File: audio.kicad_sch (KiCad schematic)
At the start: 52 parts, among them J10 NCJ6FA-H-0, J9 NCJ6FA-H-0, Q2 2N3904, Q3 2N3904, Q4 2N3906, Q5 2N3906, U10 OPA1656ID, U11 LM2903, U8 THAT1246, U9 THAT1246

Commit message: starting on output
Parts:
- C20, C22, C24, C26: value 10u -> C
- C21, C23, C25, C27, C28, C30, C32, C33: value 100n -> C
- C29, C31: value 1n -> C
- C34, C35, C36, C37: value 47u -> C
- Q2, Q3, Q4, Q5: footprint Package_TO_SOT_SMD:SOT-23 -> Package_TO_SOT_THT:TO-92_Inline
- R19, R20, R27, R30, R31, R34: value 10k 1% -> R
- R21, R22: value 12k 1% -> R
- R23, R24: value 3k3 -> R
- R25, R26: value 1k -> R
- R28, R29, R32, R33: value 1k5 1% -> R
- RV5, RV6: value 10k -> R_Potentiometer_Trim
- TP1: value IN-R -> TestPoint
- TP2: value IN-L -> TestPoint
- TP3: value +LCLAMP -> TestPoint
- TP4: value -LCLAMP -> TestPoint
- TP5: value +RCLAMP -> TestPoint
- TP6: value -RCLAMP -> TestPoint
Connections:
- net +12VA: no longer U8.7 (Vcc/V+), U9.7 (Vcc/V+)
- net GND: now also U8.7 (Vcc/V+), U9.7 (Vcc/V+); no longer U8.1 (Ref), U9.1 (Ref)
- net at J10.3, J10.R: no longer U9.2 (In-)
- net at J10.2, J10.T: no longer U9.3 (In+)
- net at J9.2, J9.T: no longer U8.3 (In+)
- net at J9.3, J9.R: no longer U8.2 (In-)

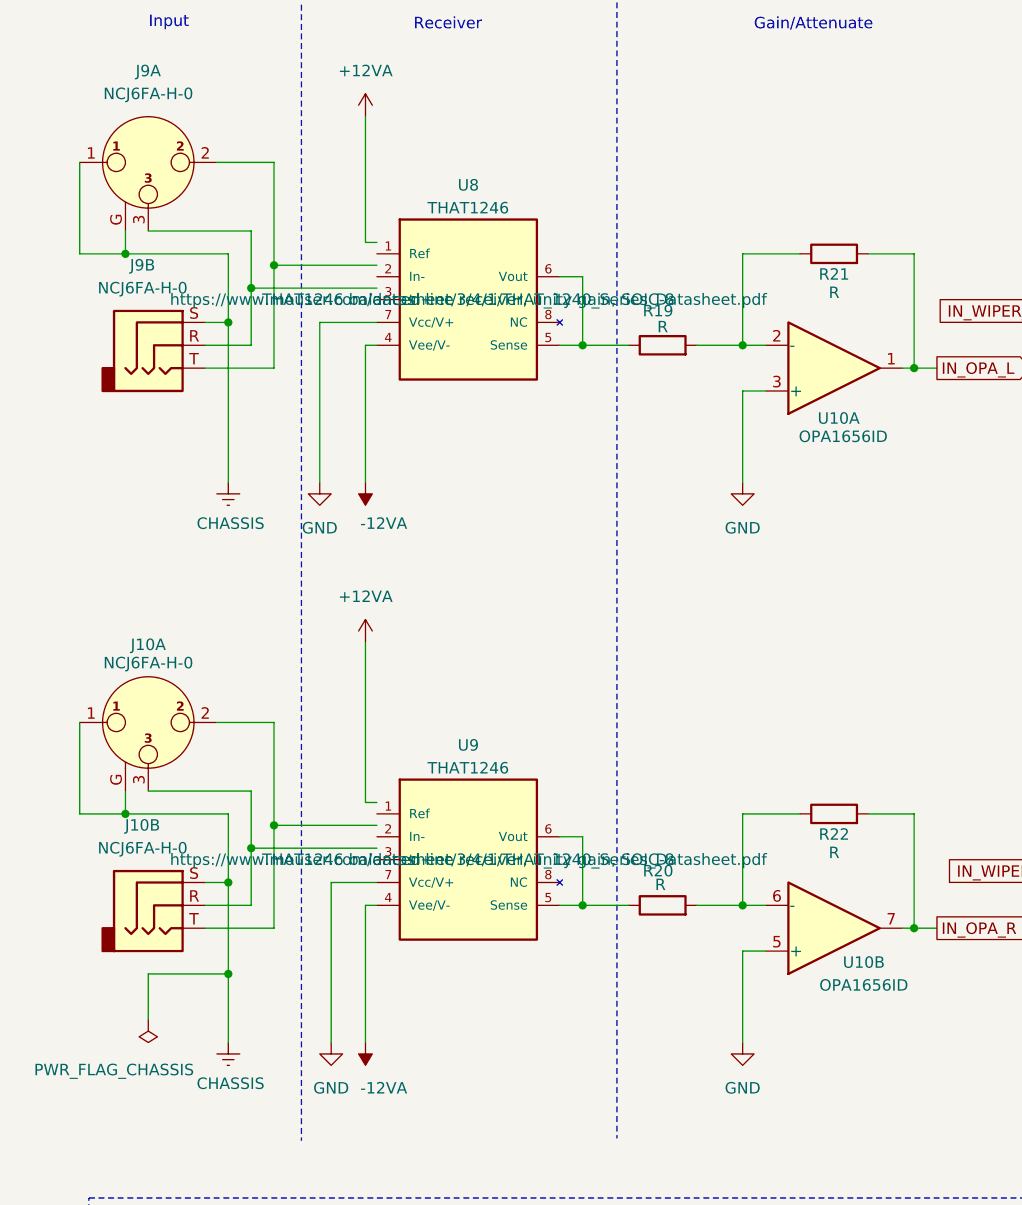
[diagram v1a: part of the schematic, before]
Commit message: daughterboard added
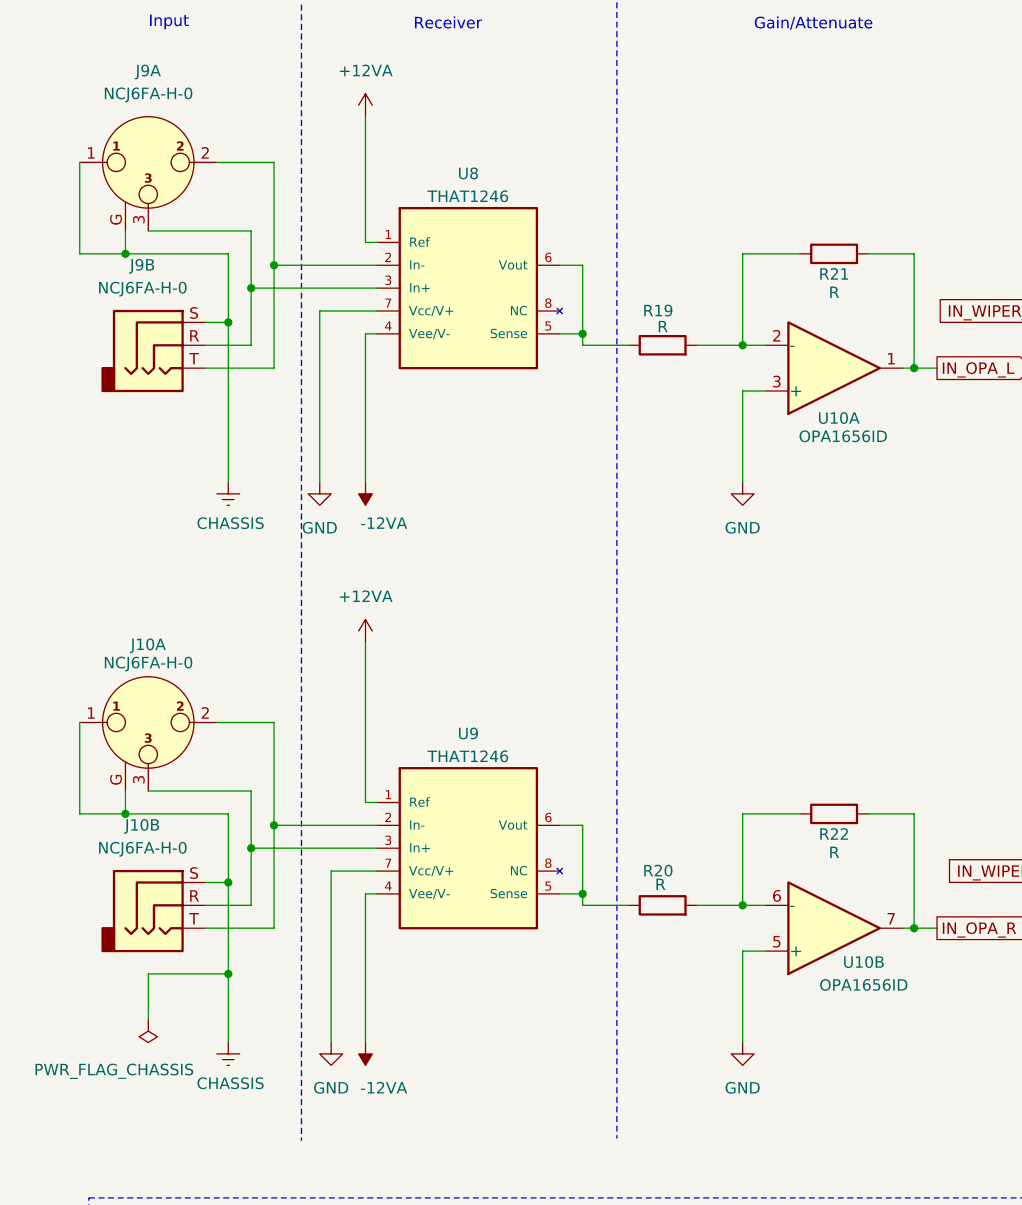
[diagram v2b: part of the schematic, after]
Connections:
- net +12VA: now also U8.1 (Ref), U9.1 (Ref)
- net at J10.3, J10.R: now also U9.3 (In+)
- net at J10.2, J10.T: now also U9.2 (In-)
- net at J9.2, J9.T: now also U8.2 (In-)
- net at J9.3, J9.R: now also U8.3 (In+)
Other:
- moved on the sheet: U8, U9
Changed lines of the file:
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@@
 	)
 	(junction
-		(at 72.39 53.34)
-		(diameter 0)
-		(color 0 0 0 0)
-	)
-	(junction
 		(at 198.12 49.53)
 		(diameter 0)
@@
 	)
 	(junction
-		(at 72.39 115.57)
-		(diameter 0)
-		(color 0 0 0 0)
-	)
-	(junction
 		(at 21.59 105.41)
 		(diameter 0)
@@
 	)
 	(junction
+		(at 72.39 52.07)
+		(diameter 0)
+		(color 0 0 0 0)
+	)
+	(junction
 		(at 238.76 39.37)
 		(diameter 0)
@@
 	)
 	(junction
+		(at 72.39 114.3)
+		(diameter 0)
+		(color 0 0 0 0)
+	)
+	(junction
 		(at 229.87 151.13)
 		(diameter 0)
@@
 	(wire
 		(pts
-			(xy 69.85 107.95) (xy 72.39 107.95)
+			(xy 69.85 106.68) (xy 72.39 106.68)
 		)
 		(stroke
@@
 	(wire
 		(pts
+			(xy 72.39 52.07) (xy 72.39 53.34)
+		)
+		(stroke
+			(width 0)
+			(type default)
+		)
+	)
+	(wire
+		(pts
 			(xy 251.46 140.97) (xy 251.46 142.24)
 		)
@@
 	(wire
 		(pts
-			(xy 44.45 113.03) (xy 44.45 130.81)
+			(xy 44.45 111.76) (xy 44.45 130.81)
 		)
 		(stroke
@@
 	(wire
 		(pts
-			(xy 72.39 107.95) (xy 72.39 115.57)
+			(xy 72.39 106.68) (xy 72.39 114.3)
 		)
 		(stroke
@@
 	(wire
 		(pts
-			(xy 69.85 53.34) (xy 72.39 53.34)
+			(xy 69.85 52.07) (xy 72.39 52.07)
 		)
 		(stroke
@@
 	(wire
 		(pts
-			(xy 49.53 113.03) (xy 44.45 113.03)
+			(xy 49.53 111.76) (xy 44.45 111.76)
 		)
 		(stroke
@@
 	(wire
 		(pts
-			(xy 48.26 115.57) (xy 49.53 115.57)
+			(xy 48.26 114.3) (xy 49.53 114.3)
 		)
 		(stroke
@@
 	(wire
 		(pts
-			(xy 43.18 50.8) (xy 43.18 68.58)
+			(xy 43.18 49.53) (xy 43.18 68.58)
 		)
 		(stroke
@@
 	(wire
 		(pts
-			(xy 69.85 45.72) (xy 72.39 45.72)
+			(xy 69.85 44.45) (xy 72.39 44.45)
 		)
 		(stroke
@@
 	(wire
 		(pts
-			(xy 48.26 130.81) (xy 48.26 115.57)
+			(xy 48.26 130.81) (xy 48.26 114.3)
 		)
 		(stroke
@@
 	(wire
 		(pts
-			(xy 48.26 53.34) (xy 49.53 53.34)
+			(xy 48.26 52.07) (xy 49.53 52.07)
 		)
 		(stroke
@@
 	(wire
 		(pts
-			(xy 49.53 50.8) (xy 43.18 50.8)
+			(xy 49.53 49.53) (xy 43.18 49.53)
 		)
 		(stroke
@@
 	(wire
 		(pts
-			(xy 72.39 45.72) (xy 72.39 53.34)
+			(xy 72.39 44.45) (xy 72.39 52.07)
 		)
 		(stroke
@@
 	(wire
 		(pts
+			(xy 72.39 114.3) (xy 72.39 115.57)
+		)
+		(stroke
+			(width 0)
+			(type default)
+		)
+	)
+	(wire
+		(pts
 			(xy 35.56 102.87) (xy 24.13 102.87)
 		)
@@
 	(wire
 		(pts
-			(xy 69.85 115.57) (xy 72.39 115.57)
+			(xy 69.85 114.3) (xy 72.39 114.3)
 		)
 		(stroke
@@
 	(wire
 		(pts
-			(xy 48.26 68.58) (xy 48.26 53.34)
+			(xy 48.26 68.58) (xy 48.26 52.07)
 		)
 		(stroke
@@
 	(symbol
 		(lib_id "daisy-studio:THAT1246")
-		(at 59.69 110.49 0)
+		(at 59.69 109.22 0)
 		(unit 1)
 		(exclude_from_sim no)
@@
 		(dnp no)
 		(property "Reference" "U9"
-			(at 59.69 97.79 0)
+			(at 59.69 96.52 0)
 			(effects
 				(font
@@
 		)
 		(property "Value" "THAT1246"
-			(at 59.69 100.33 0)
+			(at 59.69 99.06 0)
 			(effects
 				(font
@@
 		)
 		(property "Footprint" "Package_SO:SOIC-8_3.9x4.9mm_P1.27mm"
-			(at 59.69 123.19 0)
+			(at 59.69 121.92 0)
 			(effects
 				(font
@@
 		)
 		(property "Datasheet" "https://www.mouser.com/datasheet/3/4/1/THAT_1240_Series_Datasheet.pdf"
-			(at 59.69 110.49 0)
+			(at 59.69 109.22 0)
 			(effects
 				(font
 					(size 1.27 1.27)
 				)
+				(hide yes)
 			)
 		)
 		(property "Description" "THAT1246 balanced line receiver, unity gain, SOIC-8"
-			(at 59.69 110.49 0)
+			(at 59.69 109.22 0)
 			(effects
 				(font
 					(size 1.27 1.27)
 				)
+				(hide yes)
 			)
 		)
 		(property "Placement" "Near input connector. Pins 1,4 to analog ground, keep ground path short and clean."
-			(at 59.69 110.49 0)
+			(at 59.69 109.22 0)
 			(effects
 				(font
@@
 	(symbol
 		(lib_id "daisy-studio:THAT1246")
-		(at 59.69 48.26 0)
+		(at 59.69 46.99 0)
 		(unit 1)
 		(exclude_from_sim no)
@@
 		(dnp no)
 		(property "Reference" "U8"
-			(at 59.69 35.56 0)
+			(at 59.69 34.29 0)
 			(effects
 				(font
@@
 		)
 		(property "Value" "THAT1246"
-			(at 59.69 38.1 0)
+			(at 59.69 36.83 0)
 			(effects
 				(font
@@
 		)
 		(property "Footprint" "Package_SO:SOIC-8_3.9x4.9mm_P1.27mm"
-			(at 59.69 60.96 0)
+			(at 59.69 59.69 0)
 			(effects
 				(font
@@
 		)
 		(property "Datasheet" "https://www.mouser.com/datasheet/3/4/1/THAT_1240_Series_Datasheet.pdf"
-			(at 59.69 48.26 0)
+			(at 59.69 46.99 0)
 			(effects
 				(font
 					(size 1.27 1.27)
 				)
+				(hide yes)
 			)
 		)
 		(property "Description" "THAT1246 balanced line receiver, unity gain, SOIC-8"
-			(at 59.69 48.26 0)
+			(at 59.69 46.99 0)
 			(effects
 				(font
 					(size 1.27 1.27)
 				)
+				(hide yes)
 			)
 		)
 		(property "Placement" "Near input connector. Pins 1,4 to analog ground, keep ground path short and clean."
-			(at 59.69 48.26 0)
+			(at 59.69 46.99 0)
 			(effects
 				(font

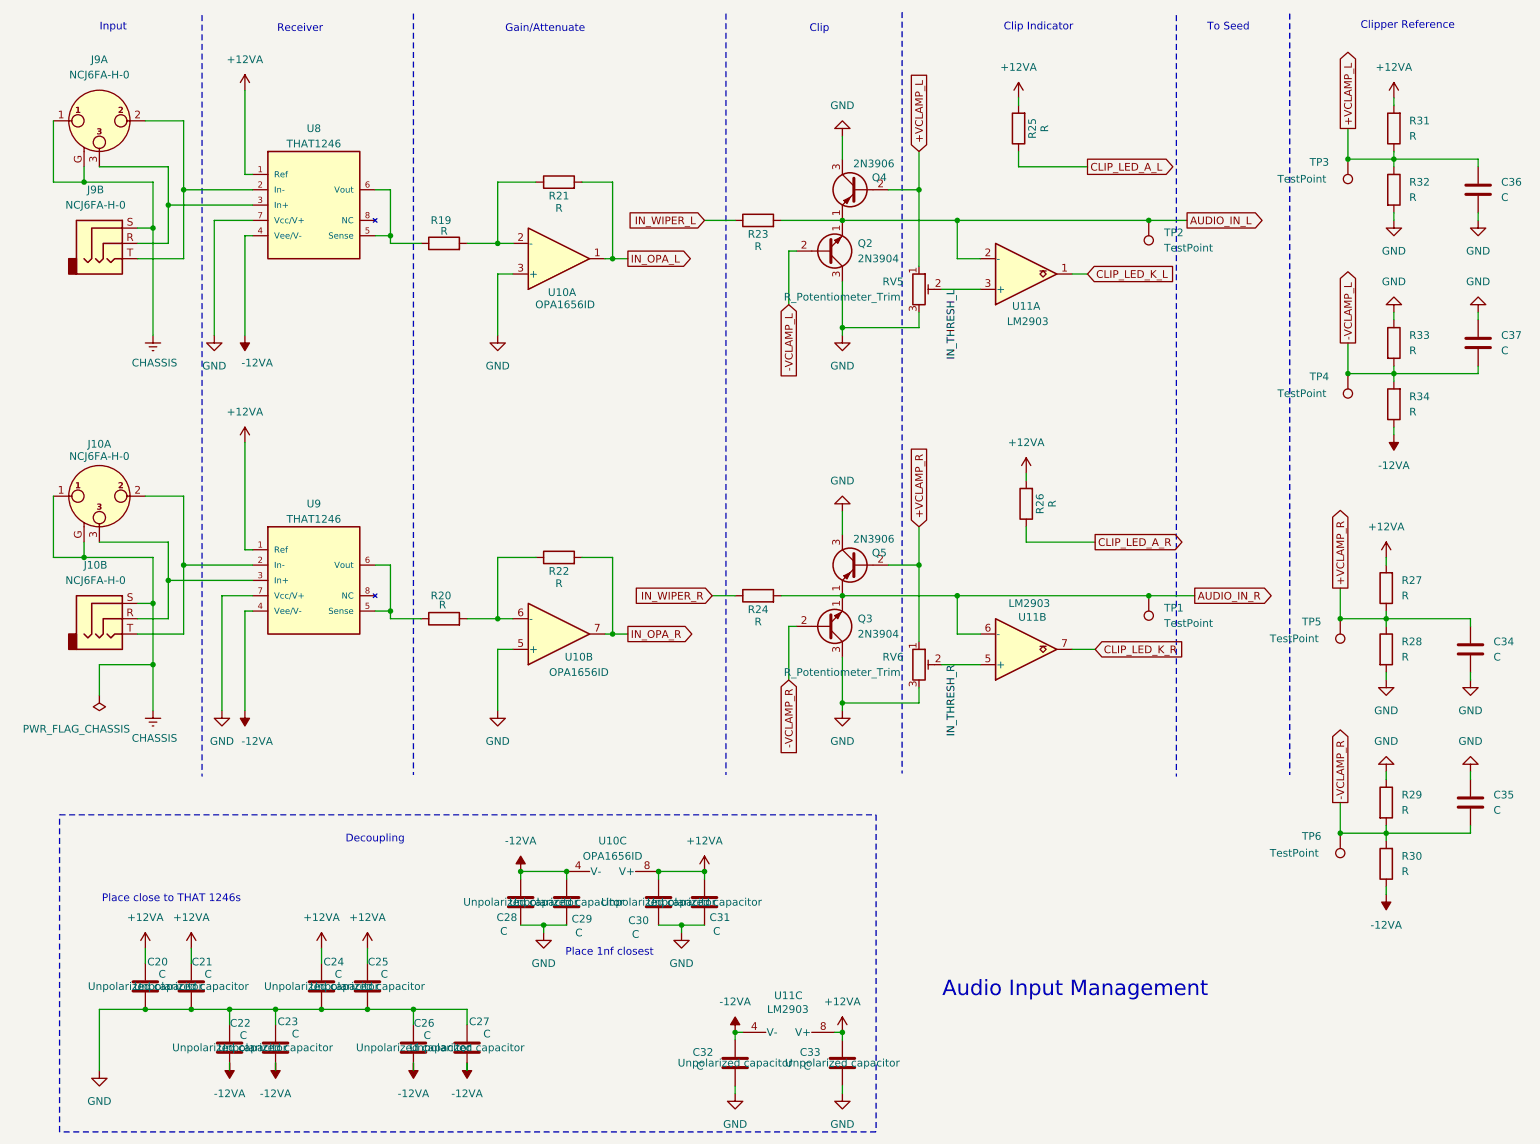
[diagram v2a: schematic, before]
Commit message: WIP trying to fix symbols and finish daughterboard
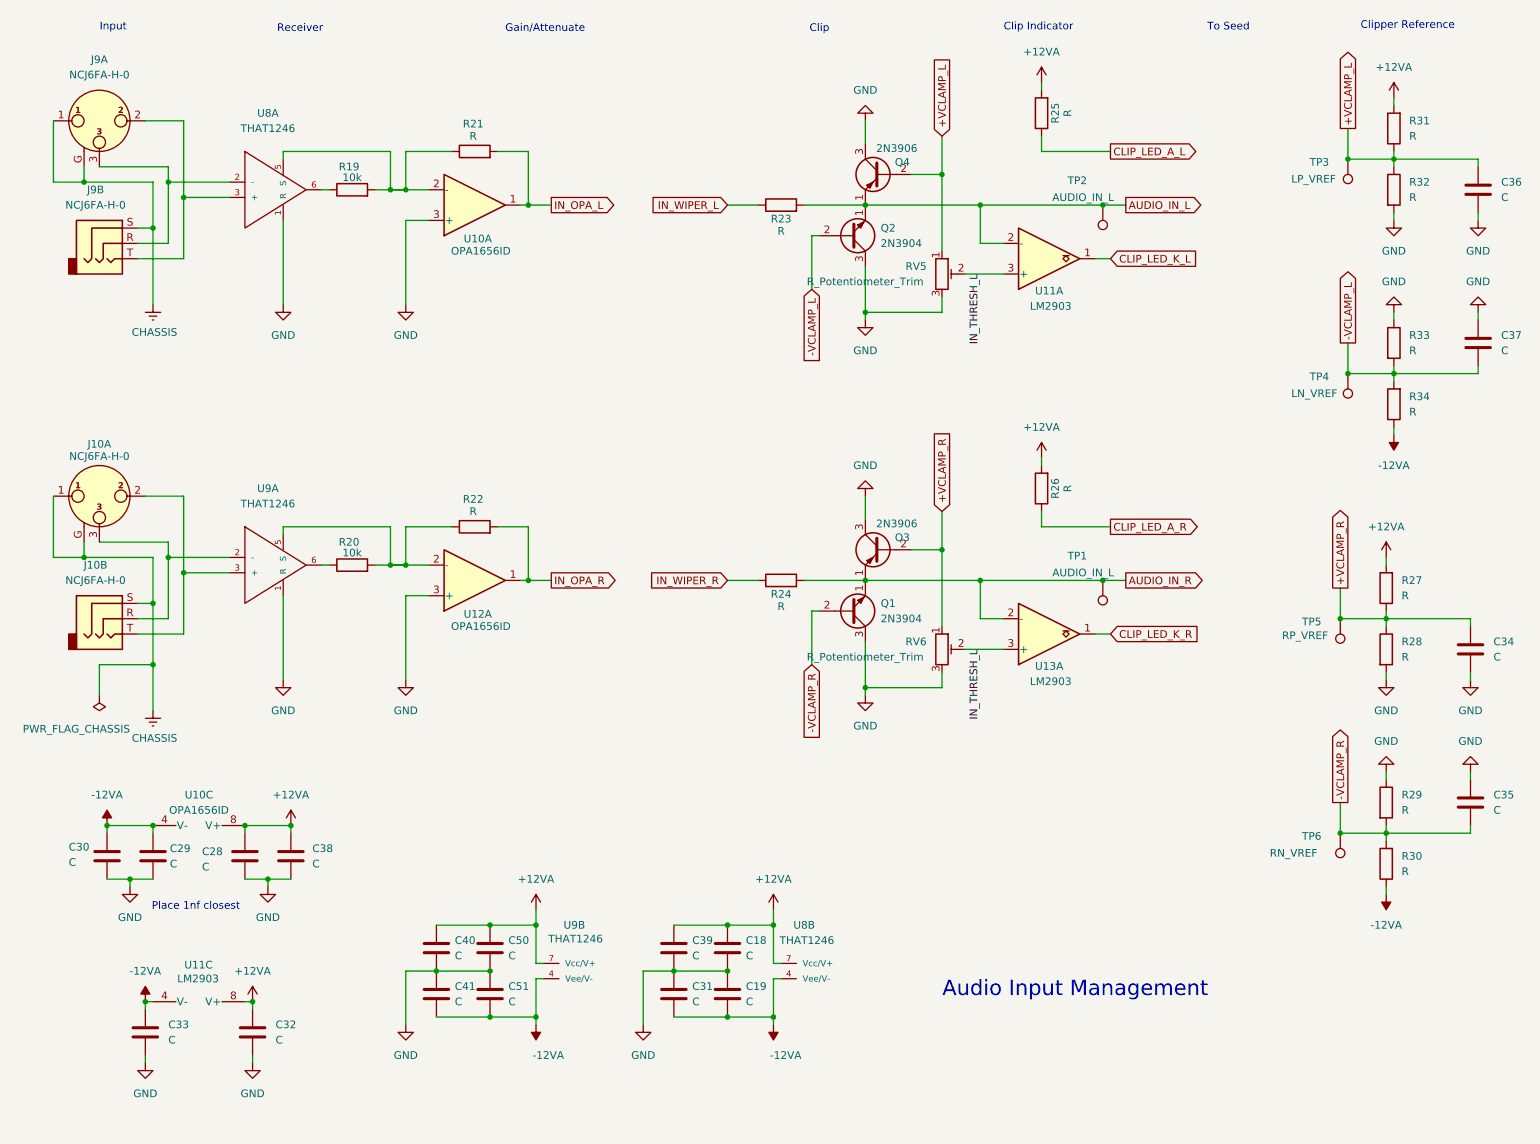
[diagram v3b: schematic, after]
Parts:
- removed C20, C21, C22, C23, C24, C25, C26, C27: C, Capacitor_SMD:C_0805_2012Metric, symbol Device:C
- removed Q3: 2N3904, Package_TO_SOT_THT:TO-92_Inline, symbol Transistor_BJT:2N3904
- removed Q5: 2N3906, Package_TO_SOT_THT:TO-92_Inline, symbol Transistor_BJT:2N3906
- removed unit 2 of U10
- removed unit 2 of U11
- removed U9: THAT1246, Package_SO:SOIC-8_3.9x4.9mm_P1.27mm, symbol daisy-studio:THAT1246
- added C18, C19, C38, C39, C40, C41, C50, C51: C, symbol Device:C
- added Q1: 2N3904, Package_TO_SOT_THT:TO-92_Inline, symbol Transistor_BJT:2N3904
- added Q3: 2N3906, Package_TO_SOT_THT:TO-92_Inline, symbol Transistor_BJT:2N3906
- added U12: OPA1656ID, Package_SO:SOIC-8_3.9x4.9mm_P1.27mm, symbol Amplifier_Operational:OPA1656ID
- added U13: LM2903, symbol Comparator:LM2903
- added U9: THAT1246, Package_SO:SOIC-8_3.9x4.9mm_P1.27mm, symbol daisy-studio:THAT1246
- C28, C29, C30, C31, C32, C33: footprint Capacitor_SMD:C_0805_2012Metric -> (none)
- R19, R20: value R -> 10k
- TP1, TP2: value TestPoint -> AUDIO_IN_L
- TP3: value TestPoint -> LP_VREF
- TP4: value TestPoint -> LN_VREF
- TP5: value TestPoint -> RP_VREF
- TP6: value TestPoint -> RN_VREF
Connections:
- net IN_THRESH_R is gone; now on net IN_THRESH_L: RV6.2
- net +12VA: now also C28.1, C32.1, U8.7 (Vcc/V+), C18.1, C38.1, C39.1, C40.1, C50.1, U9.7 (Vcc/V+); no longer C30.1, C31.1, C33.1, U8.1 (Ref)
- net +VCLAMP_R: now also Q3.2 (B)
- net -12VA: now also C30.1, C31.2, C33.1, C19.2, C41.2, C51.2, U9.4 (Vee/V-); no longer C28.1, C32.1
- net -VCLAMP_R: now also Q1.2 (B)
- net AUDIO_IN_R: now also Q1.1 (E), Q3.1 (E), U13.2 (-)
- net CLIP_LED_K_R: now also U13.1
- net GND: now also C31.1, U8.1 (R), C18.2, C19.1, C38.2, C39.2, C40.2, C41.1, C50.2, C51.1, Q1.3 (C), Q3.3 (C), U12.3 (+), U9.1 (R); no longer C31.2, U8.7 (Vcc/V+)
- net IN_OPA_R: now also U12.1
- net IN_THRESH_L: now also U13.3 (+)
- net at J10.3, J10.R: now also U9.2 (-)
- net at J10.2, J10.T: now also U9.3 (+)
- net at R20.2, R22.1: now also U12.2 (-), U9.5 (S)
- net at J9.2, J9.T: now also U8.3 (+); no longer U8.2 (In-)
- net at J9.3, J9.R: now also U8.2 (-); no longer U8.3 (In+)
- net at R20.1: now also U9.6
- net at R19.1, U8.6: no longer U8.5 (Sense)
- net at R19.2, R21.1, U10.2 (-): now also U8.5 (S)
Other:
- note removed: "Decoupling"
- note removed: "Place close to THAT 1246s"
- moved on the sheet: Q2, Q4, R19, R21, R23, R25, RV5, TP2, U10A, U10C, U11A, U11C

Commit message: WIP adding values
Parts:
- removed U12: OPA1656ID, Package_SO:SOIC-8_3.9x4.9mm_P1.27mm, symbol Amplifier_Operational:OPA1656ID
- removed U13: LM2903, symbol Comparator:LM2903
- added unit 2 of U10
- added unit 1 of U11
- added unit 1 of U8
- added unit 2 of U9
- C18, C19, C30, C32, C33, C38, C50, C51: value C -> 100n
- C28, C29: value C -> 1n
- C31, C39, C40, C41: value C -> 10u
- C34, C35, C36, C37: value C -> 47u
- R21, R22: value R -> 12k 1%
- R23, R24: value R -> 3.3k 1%
- R25, R26: value R -> 1k
- R27, R30, R31, R34: value R -> 10k 1%
- R28, R29, R32, R33: value R -> 1.5k 1%
- RV5, RV6: value R_Potentiometer_Trim -> 10k
- TP1: value AUDIO_IN_L -> AUDIO_IN_R
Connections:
- net +12VA: now also U9.7 (Vcc/V+); no longer U9.7 (Vcc/V+)
- net -12VA: now also U9.4 (Vee/V-); no longer U9.4 (Vee/V-)
- net AUDIO_IN_L: now also U11.2 (-); no longer U11.2 (-)
- net AUDIO_IN_R: now also U11.6 (-)
- net CLIP_LED_K_L: now also U11.1; no longer U11.1
- net CLIP_LED_K_R: now also U11.7
- net GND: now also U10.5 (+), U8.1 (R); no longer U8.1 (R)
- net IN_OPA_R: now also U10.7
- net IN_THRESH_L: now also U11.5 (+), U11.3 (+); no longer U11.3 (+)
- net at J9.2, J9.T: now also U8.3 (+); no longer U8.3 (+)
- net at J9.3, J9.R: now also U8.2 (-); no longer U8.2 (-)
- net at R20.2, R22.1, U9.5 (S): now also U10.6 (-)
- net at R19.2, R21.1, U10.2 (-): now also U8.5 (S); no longer U8.5 (S)
- net at R19.1: now also U8.6; no longer U8.6
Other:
- moved on the sheet: U11B
